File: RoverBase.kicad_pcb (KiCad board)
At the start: 2 copper layers, 106 x 118 mm, 59 parts, among them J1 Conn_01x02, J2 Conn_01x06, J3 Conn_01x04, J4 Conn_01x02, J5 Conn_01x03, J6 Conn_02x03_Counter_Clockwise, J7 Conn_02x03_Counter_Clockwise, SW1 SW_SPDT, SW2 SW_SPDT, SW3 SW_SPDT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

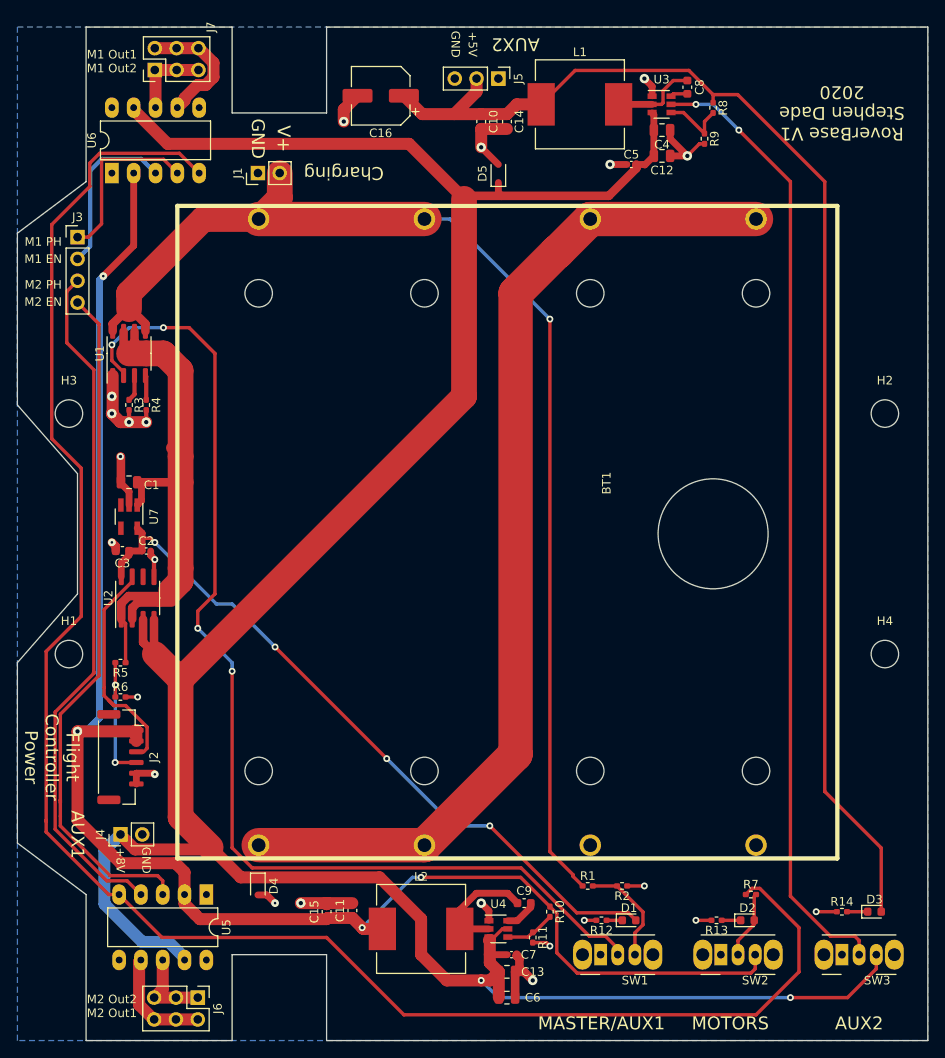
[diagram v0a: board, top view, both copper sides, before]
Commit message: Fixes from V1 testing
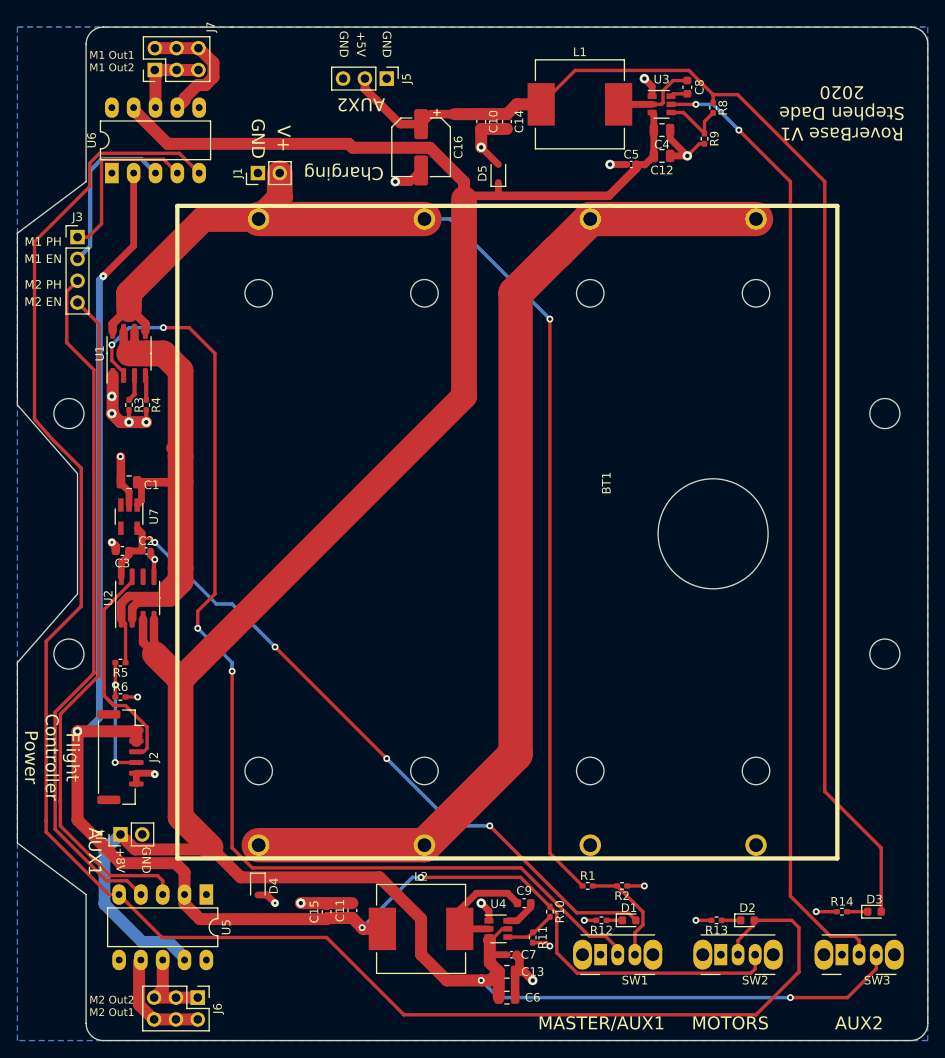
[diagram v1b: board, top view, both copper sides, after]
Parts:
- removed R7: 10k, Resistor_SMD:R_0402_1005Metric_Pad0.72x0.64mm_HandSolder
- H1, H2, H3, H4: footprint MountingHole:MountingHole_3.2mm_M3_ISO7380 -> MountingHole:MountingHole_3.5mm
- R11, R9: value 10.0k -> 10k
- moved J5 13.0 mm to (167.6, 35.0)
- moved C16 7.62 mm to (171.6, 43.0), turned to 270 degrees
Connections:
- J5 pad 1: (no net) -> GND
- U5 pad 5: Net-(R7-Pad1) -> Net-(D2-Pad2)
- U6 pad 5: Net-(R7-Pad1) -> Net-(D2-Pad2)
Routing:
- net Net-(R7-Pad1): track 209.2 -> 0.00 mm
- net Net-(D2-Pad2): track 7.87 -> 212.8 mm
- net Net-(C10-Pad1): track 151.2 -> 153.1 mm
- net /VIN: track 314.9 -> 316.1 mm
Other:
- outline, holes or cut-outs redrawn

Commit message: Updated inductor footprint
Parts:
- L1, L2: footprint Inductor_SMD:L_Vishay_IHLP-4040 -> Vishay_IHLP-3232:L_Vishay_IHLP-3232

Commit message: Better power supply placement
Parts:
- added J8: Conn_01x01, Connector_Pin:Pin_D1.3mm_L11.0mm, F.Cu at (155.6, 43.0)
- J1: value Conn_01x02 -> Conn_01x01; footprint Connector_PinHeader_2.54mm:PinHeader_1x02_P2.54mm_Vertical -> Connector_Pin:Pin_D1.3mm_L11.0mm
- moved D4 11.0 mm to (163.6, 129.0)
- moved J1 3.16 mm to (151.6, 43.0), turned to 0 degrees
- moved C11 2.37 mm to (165.6, 133.1)
- moved C15 2.30 mm to (162.6, 133.1)
- moved L2 1.00 mm to (172.6, 134.0)
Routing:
- net /VIN: track 316.5 -> 319.1 mm
- net Net-(BT1-Pad3): track 140.2 -> 142.4 mm
- net /FC_5V: track 187.1 -> 188.9 mm
- net GND: track 79.5 -> 78.0 mm, vias 23 -> 22

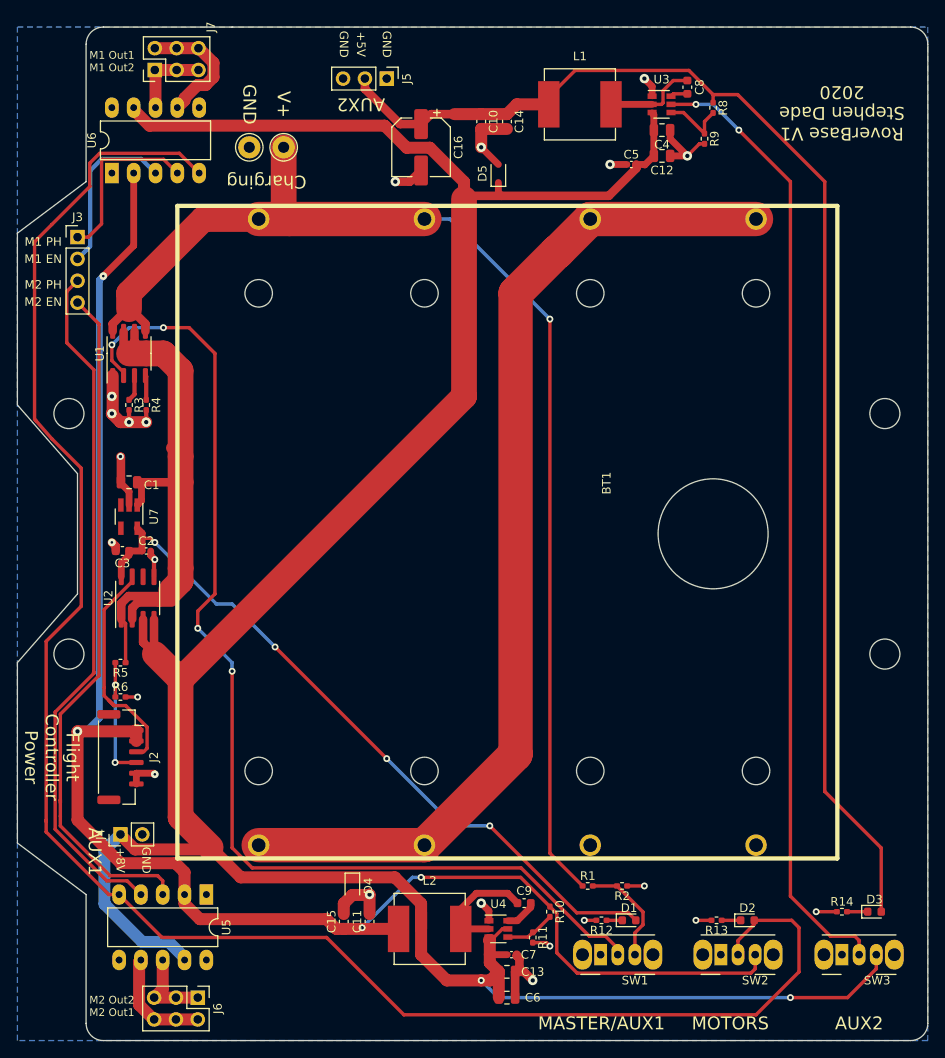
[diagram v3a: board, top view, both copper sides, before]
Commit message: Updated motor controllers
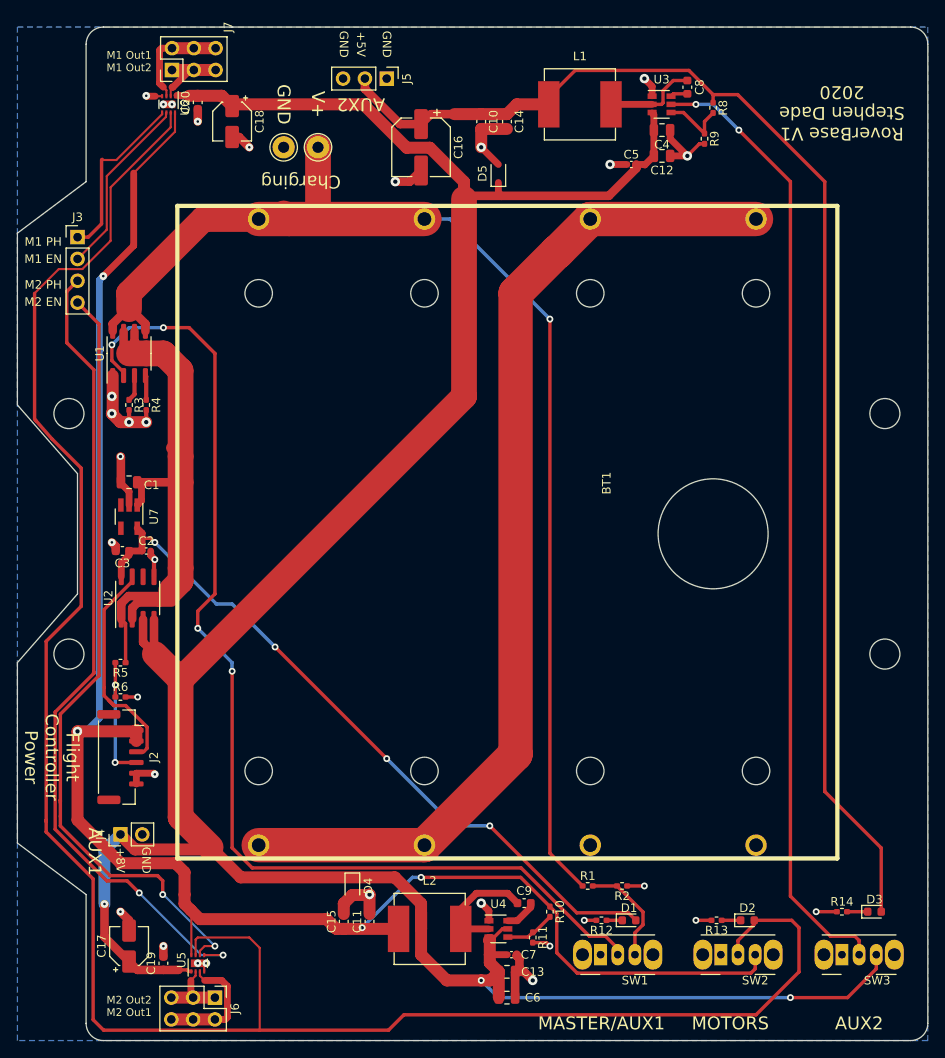
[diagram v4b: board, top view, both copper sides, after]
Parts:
- added C17: 10uF 16V, Capacitor_SMD:CP_Elec_4x5.4, F.Cu at (137.6, 136.0)
- added C18: 10uF 16V, Capacitor_SMD:CP_Elec_4x5.4, F.Cu at (149.6, 40.0)
- added C19: 100nF, 25V, Capacitor_SMD:C_0603_1608Metric, F.Cu at (141.6, 138.0)
- added C20: 100nF, 25V, Capacitor_SMD:C_0603_1608Metric, F.Cu at (145.6, 37.8)
- U5, U6: footprint Package_DIP:DIP-10_W7.62mm_LongPads -> Package_SON:WSON-8-1EP_2x2mm_P0.5mm_EP0.9x1.6mm
- moved U6 10.4 mm to (142.2, 38.0), turned to 270 degrees
- moved U5 8.06 mm to (145.6, 138.0), turned to 90 degrees
- moved J1 4.00 mm to (155.6, 43.0)
- moved J8 4.00 mm to (159.6, 43.0)
- moved J6 2.00 mm to (147.6, 142.0)
- moved J7 2.00 mm to (142.6, 34.0)
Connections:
- U5 pad 1: GND -> /VIN
- U5 pad 2: /FC_5V -> Net-(J6-Pad1)
- U5 pad 3: Net-(J3-Pad4) -> Net-(J6-Pad2)
- U5 pad 4: Net-(J3-Pad3) -> GND
- U5 pad 5: Net-(D2-Pad2) -> Net-(J3-Pad3)
- U5 pad 6: (no net) -> Net-(J3-Pad4)
- U5 pad 7: Net-(J6-Pad2) -> Net-(D2-Pad2)
- U5 pad 8: Net-(J6-Pad1) -> /FC_5V
- U5 pad 9: /VIN -> GND
- U6 pad 1: GND -> /VIN
- U6 pad 2: /FC_5V -> Net-(J7-Pad1)
- U6 pad 3: Net-(J3-Pad2) -> Net-(J7-Pad2)
- U6 pad 4: Net-(J3-Pad1) -> GND
- U6 pad 5: Net-(D2-Pad2) -> Net-(J3-Pad1)
- U6 pad 6: (no net) -> Net-(J3-Pad2)
- U6 pad 7: Net-(J7-Pad2) -> Net-(D2-Pad2)
- U6 pad 8: Net-(J7-Pad1) -> /FC_5V
- U6 pad 9: /VIN -> GND
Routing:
- net Net-(D2-Pad2): track 212.8 -> 240.6 mm
- net /FC_5V: track 188.9 -> 203.2 mm
- net Net-(J3-Pad3): track 81.1 -> 95.4 mm, vias 0 -> 2
- net Net-(J3-Pad4): track 80.3 -> 91.3 mm, vias 0 -> 2
- net GND: track 78.0 -> 88.7 mm, vias 22 -> 31
- net Net-(J7-Pad2): track 15.0 -> 12.4 mm
- net Net-(J6-Pad2): track 12.8 -> 14.5 mm
- net Net-(J3-Pad2): track 19.7 -> 21.3 mm
- net Net-(J6-Pad1): track 9.87 -> 8.47 mm
- net /VIN: track 319.1 -> 318.0 mm, vias 2 -> 3

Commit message: Smaller size pcb and re-layout
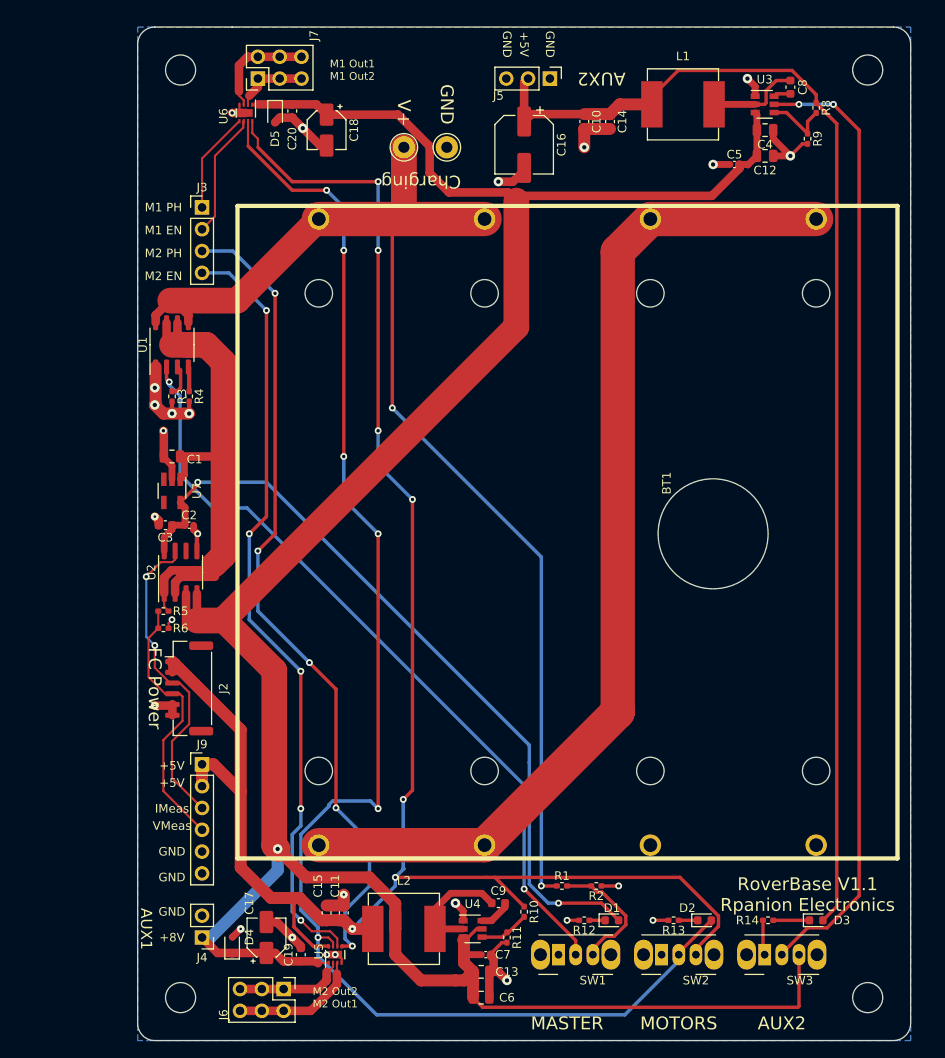
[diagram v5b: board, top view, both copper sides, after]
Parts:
- added J9: Conn_01x06, Connector_PinHeader_2.54mm:PinHeader_1x06_P2.54mm_Vertical, F.Cu at (146.1, 114.8)
- J2: footprint Connector_JST:JST_GH_SM06B-GHS-TB_1x06-1MP_P1.25mm_Horizontal -> Connector_JST:JST_GH_BM06B-GHS-TBT_1x06-1MP_P1.25mm_Vertical
- moved H1 42.1 mm to (143.6, 142.0)
- moved H3 42.1 mm to (143.6, 34.0)
- moved H2 40.0 mm to (223.6, 34.0)
- moved H4 40.0 mm to (223.6, 142.0)
- moved D5 26.9 mm to (154.6, 39.0), turned to 270 degrees
- moved J1 19.0 mm to (174.6, 43.0)
- moved J5 19.0 mm to (186.6, 35.0)
- moved C17 16.0 mm to (153.6, 135.0)
- moved C19 16.0 mm to (157.6, 137.0)
- moved U5 16.0 mm to (161.6, 137.0)
- moved D4 15.7 mm to (149.6, 136.0), turned to 90 degrees
- moved J4 15.3 mm to (146.1, 135.0), turned to 180 degrees
- moved J3 14.9 mm to (146.1, 50.0)
- moved C16 12.0 mm to (183.6, 42.7)
- moved C10 12.0 mm to (190.6, 40.0)
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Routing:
- net Net-(D2-Pad2): track 240.6 -> 171.4 mm, vias 0 -> 6
- net Net-(SW1-Pad2): track 128.8 -> 91.7 mm, vias 4 -> 2
- net /FC_5V: track 203.2 -> 224.4 mm, vias 4 -> 7
- net /VIN: track 318.0 -> 297.7 mm, vias 3 -> 1
- net Net-(J2-Pad4): track 16.0 -> 31.3 mm, vias 2 -> 0
- net Net-(C10-Pad1): track 153.1 -> 140.6 mm
- net Net-(J2-Pad3): track 26.9 -> 38.4 mm, vias 0 -> 2
- net Net-(J3-Pad1): track 20.4 -> 11.9 mm
- net Net-(C2-Pad1): track 83.7 -> 90.6 mm, vias 4 -> 2
- net Net-(J3-Pad2): track 21.3 -> 14.6 mm
- net Net-(C1-Pad1): track 67.5 -> 61.7 mm
- net Net-(J6-Pad1): track 8.47 -> 12.9 mm
- net GND: track 88.7 -> 91.8 mm, vias 31 -> 26
- net Net-(R1-Pad2): track 12.4 -> 15.0 mm
- net Net-(D3-Pad1): track 2.40 -> 4.21 mm
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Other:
- board size 106 x 118 mm -> 90 x 118 mm
- board text added: "FC Power"
- board text added: "IMeas"
- board text added: "MASTER"
- board text added: "RoverBase V1.1 Rpanion Electronics"
- board text added: "VMeas"
- board text removed: "Flight Controller Power"
- board text removed: "MASTER/AUX1"
- board text removed: "RoverBase V1 Stephen Dade 2020"

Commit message: Update board pins
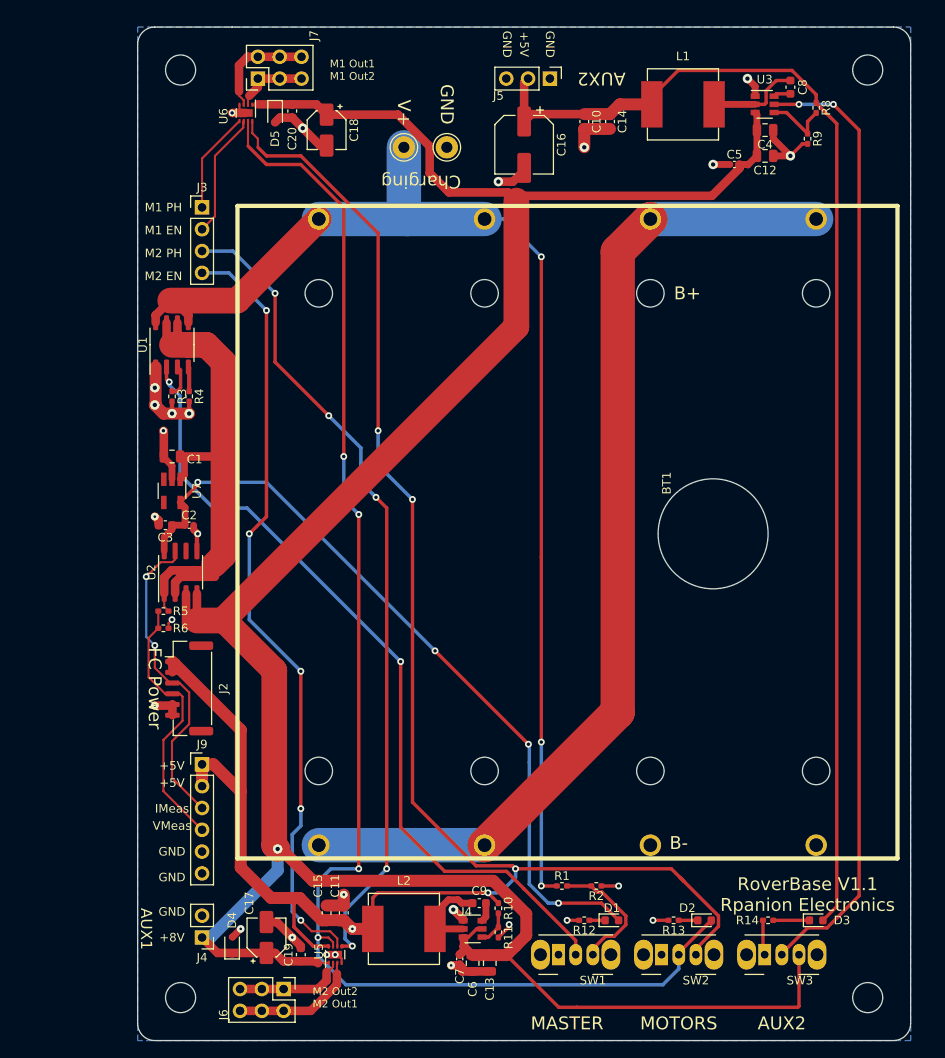
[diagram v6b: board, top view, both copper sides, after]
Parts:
- moved C6 4.12 mm to (177.6, 138.0), turned to 270 degrees
- moved C7 3.06 mm to (176.1, 137.5), turned to 270 degrees
- moved R10 3.03 mm to (180.6, 131.6)
- moved C9 2.23 mm to (178.4, 131.0)
- moved C13 1.41 mm to (179.6, 138.0), turned to 90 degrees
- moved R11 1.16 mm to (180.6, 134.4)
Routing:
- net Net-(D2-Pad2): track 171.4 -> 163.1 mm, vias 6 -> 4
- net Net-(SW1-Pad2): track 91.7 -> 95.9 mm
- net GND: track 91.8 -> 87.8 mm, vias 26 -> 27
- net Net-(BT1-Pad3): track 143.1 -> 139.5 mm, vias 2 -> 3
- net Net-(R10-Pad2): track 5.87 -> 3.98 mm
- net Net-(C9-Pad2): track 3.80 -> 2.24 mm
- net Net-(C9-Pad1): track 13.6 -> 12.9 mm
- net /FC_5V: track 224.4 -> 224.5 mm, vias 7 -> 5
- net Net-(C2-Pad1): vias 2 -> 4
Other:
- board text added: "B+"
- board text added: "B-"

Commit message: FC Power 5.1V to 5.3V
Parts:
- R10: value 56.2k -> 59k

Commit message: Cleanup and consolidate
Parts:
- C19, C20, C3: value 100nF, 25V -> 100nF, 16V; footprint Capacitor_SMD:C_0603_1608Metric -> Capacitor_SMD:C_0402_1005Metric
- moved C16 6.77 mm to (190.3, 43.2)
- moved J5 6.47 mm to (192.9, 36.5)
- moved C10 4.27 mm to (194.8, 40.4)
- moved C14 3.02 mm to (196.6, 40.4)
- moved R9 2.50 mm to (214.6, 40.5)
- moved C5 2.16 mm to (209.3, 43.2), turned to 90 degrees
- moved R8 1.75 mm to (215.8, 38.4)
- moved L1 1.36 mm to (203.2, 37.2)
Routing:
- net Net-(R8-Pad2): track 7.73 -> 3.92 mm
- net Net-(C10-Pad1): track 140.6 -> 137.9 mm
- net /VIN: track 297.6 -> 299.5 mm
- net GND: track 87.8 -> 89.2 mm, vias 27 -> 25
